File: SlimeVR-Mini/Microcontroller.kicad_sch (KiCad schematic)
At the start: 10 parts, among them SW1 SW_Push, U1 ESP32-C3-MINI-1-N4, U4 CH340N

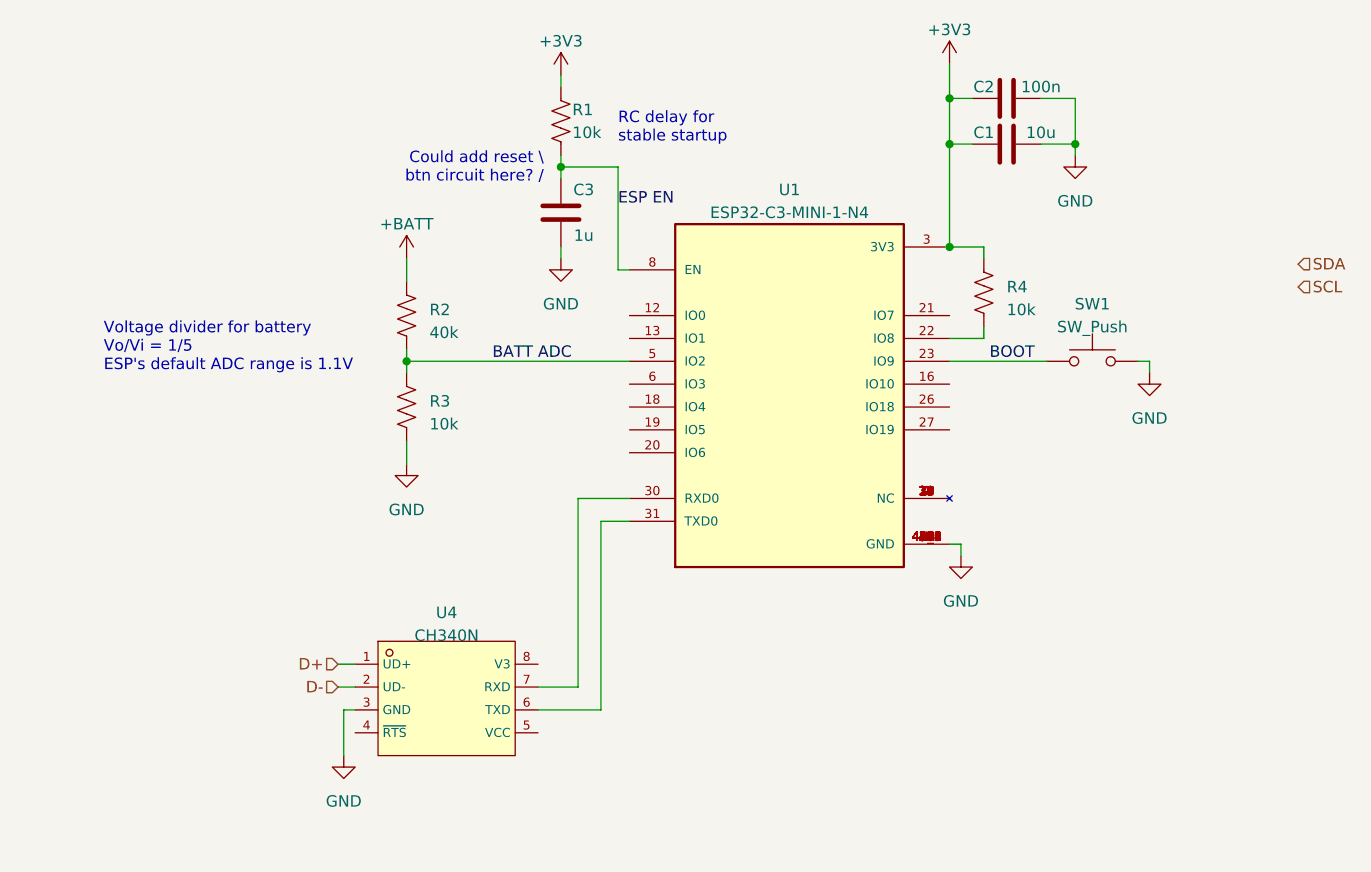
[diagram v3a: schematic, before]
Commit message: assigned footprints, finished USB-UART sch
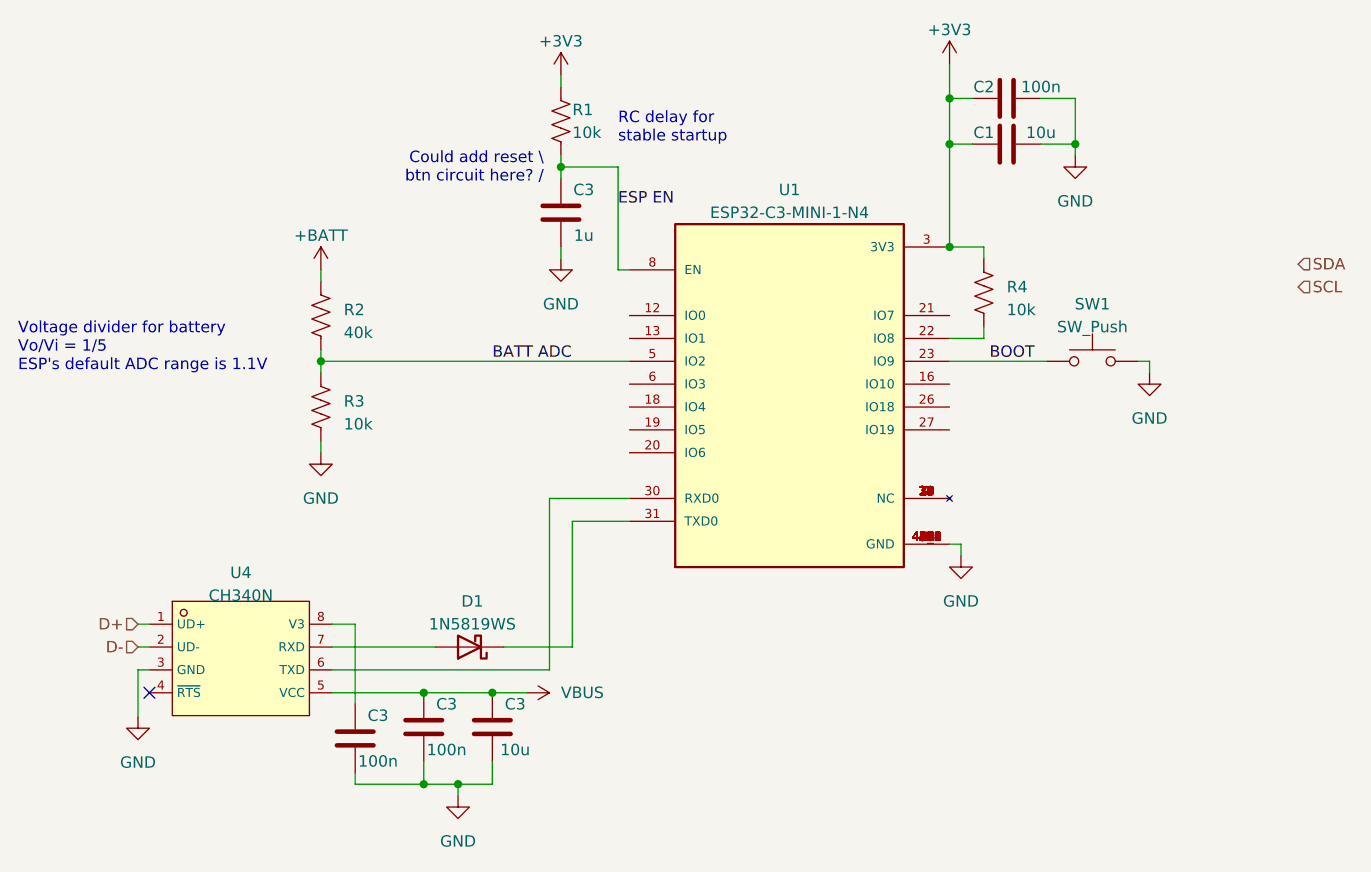
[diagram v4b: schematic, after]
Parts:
- added C3: 10u, Capacitor_SMD:C_0402_1005Metric, symbol Device:C
- added C3 (x2): 100n, Capacitor_SMD:C_0402_1005Metric, symbol Device:C
- added D1: 1N5819WS, Diode_SMD:D_SOD-323, symbol Diode:1N5819WS
- C1, C2, C3: footprint (none) -> Capacitor_SMD:C_0402_1005Metric
- R1, R2, R3, R4: footprint (none) -> Resistor_SMD:R_0402_1005Metric
- SW1: footprint (none) -> Button_Switch_SMD:SW_SPST_B3U-1000P
- U1: footprint Project Library:XCVR_ESP32-C3-MINI-1-N4 -> Project Library:ESP32-C3-MINI-1-N4
- U4: footprint easyeda2kicad:SOP-8_L4.9-W3.9-P1.27-LS6.0-BL -> Project Library:SOP-8_L4.9-W3.9-P1.27-LS6.0-BL
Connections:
- net GND: now also C3.2, C3.2, C3.2
- net at U1.30 (RXD0): now also U4.6 (TXD); no longer U4.7 (RXD)
- net at U1.31 (TXD0): now also D1.1 (K); no longer U4.6 (TXD)
- net VBUS: now reaches U4.5 (VCC)
- net VBUS: now also C3.1, C3.1
- net at U4.8 (V3): now also C3.1
- new net: D1.2 (A), U4.7 (RXD)
- no-connect marks 0 -> 1
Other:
- moved on the sheet: R2, R3, U4
